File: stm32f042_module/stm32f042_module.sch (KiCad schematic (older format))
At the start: 6 parts, among them P1 CONN_01X10, U1 STM32F042F6P6

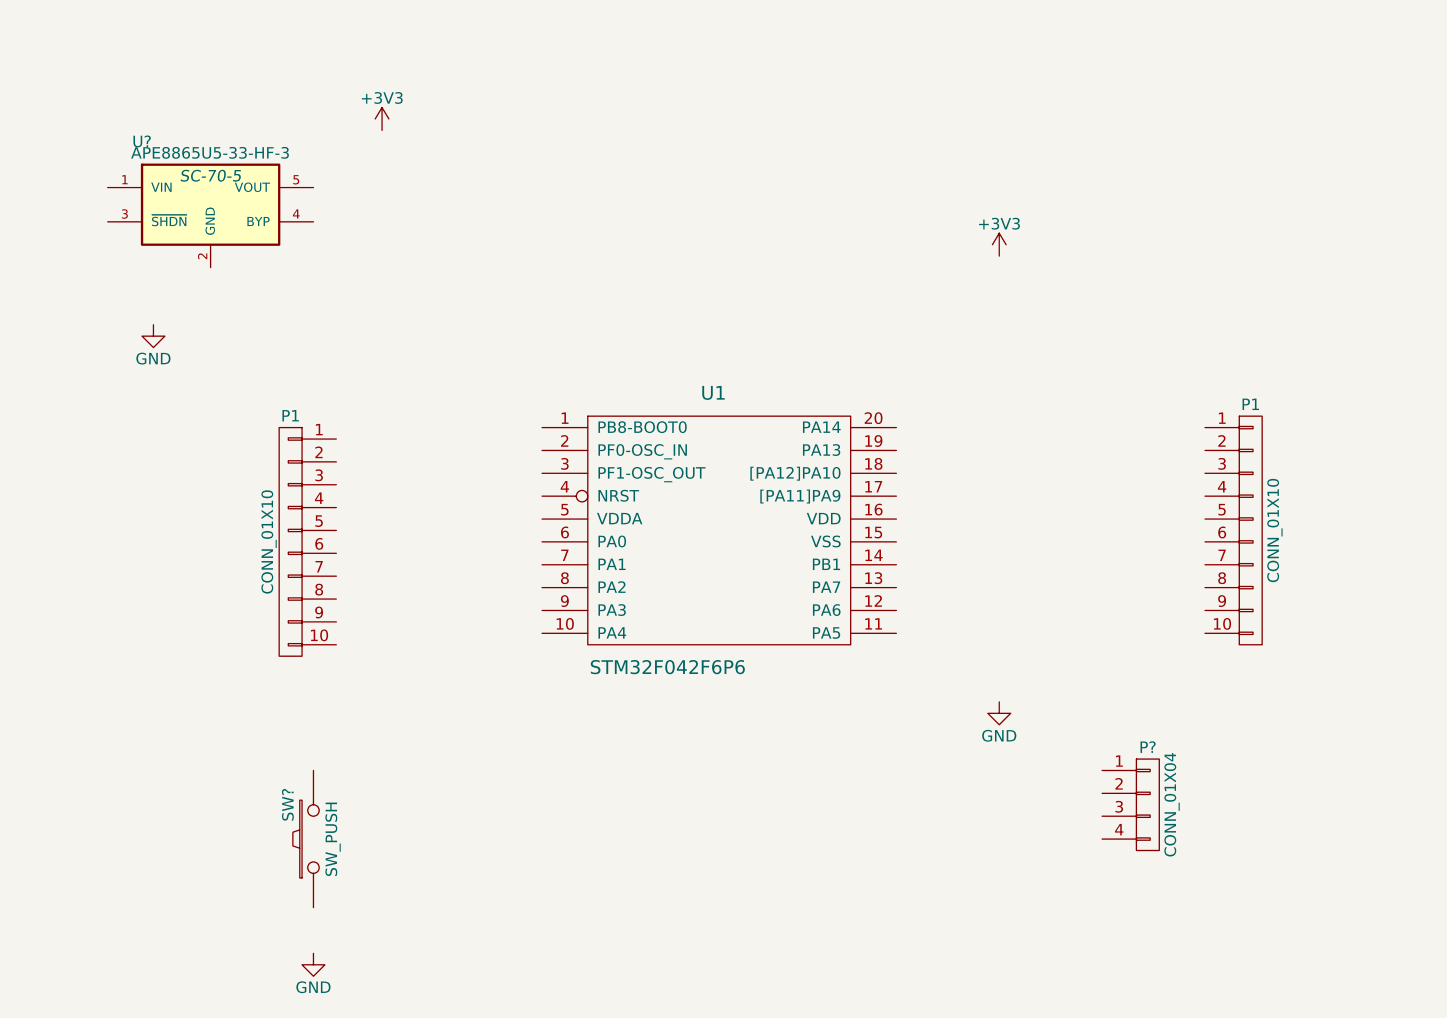
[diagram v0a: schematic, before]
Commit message: add usb conn and footprint
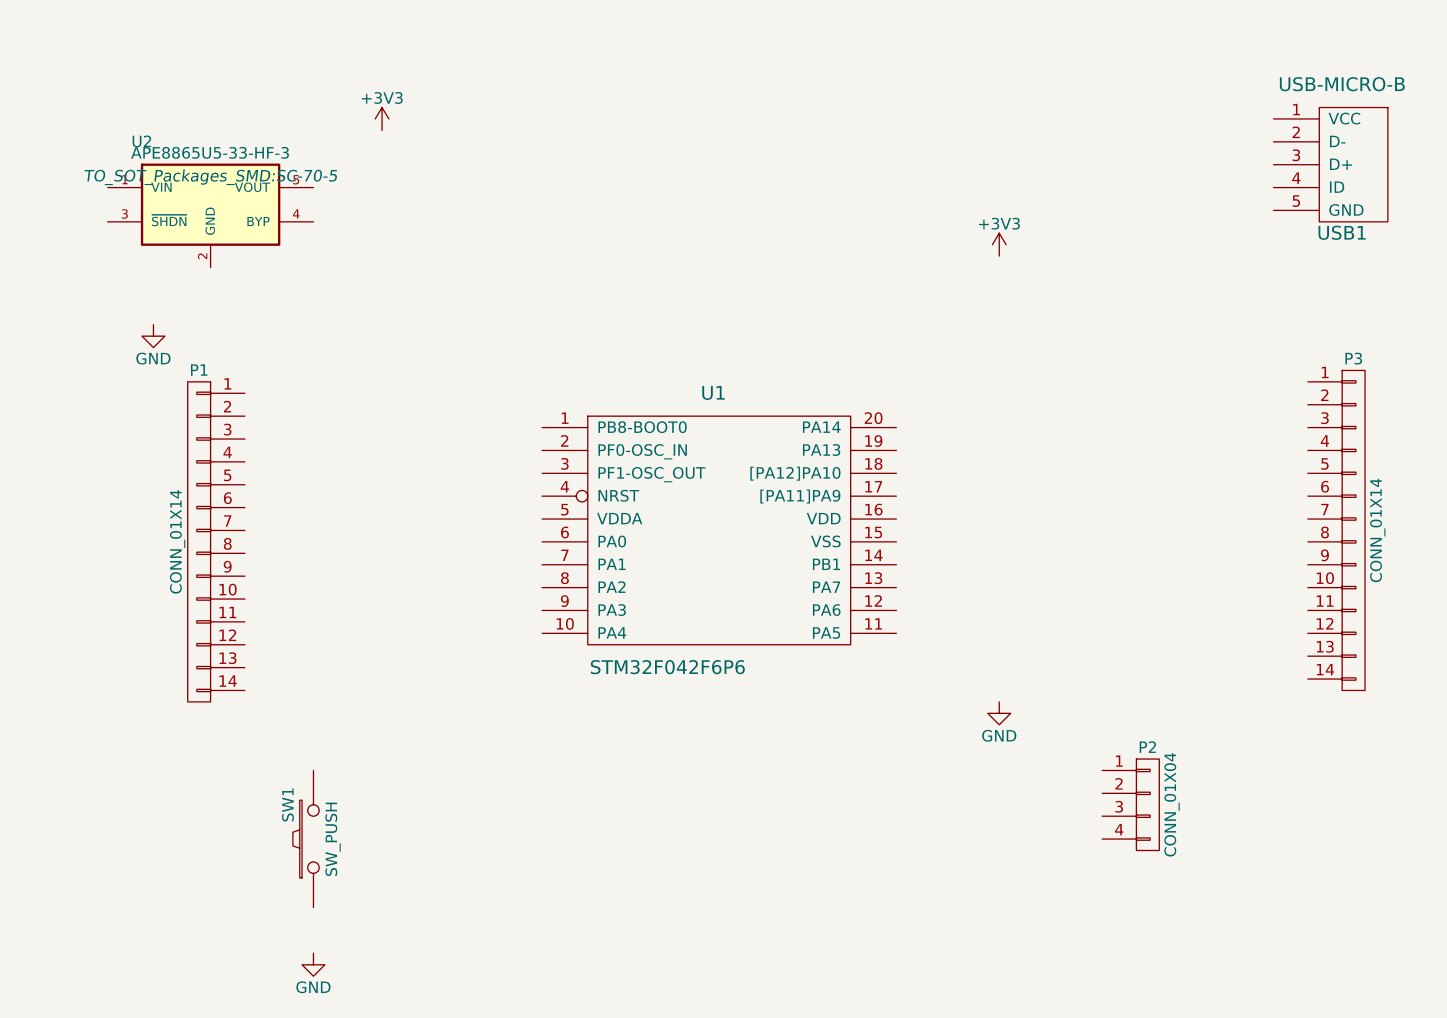
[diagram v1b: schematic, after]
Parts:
- removed P1 (x2): CONN_01X10, symbol CONN_01X10
- added P1, P3: CONN_01X14, symbol CONN_01X14
- added USB1: USB-MICRO-B, smt-other:USB-MICRO-B-SMT, symbol USB-MICRO-B
- U2: renamed from U?; footprint SC-70-5 -> TO_SOT_Packages_SMD:SC-70-5
- gave numbers to parts that had none: 2
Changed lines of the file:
@@
 LIBS:contrib
 LIBS:valves
+LIBS:stm32f042_module-cache
 EELAYER 25 0
 EELAYER END
@@
 $EndComp
 $Comp
-L CONN_01X10 P1
-U 1 1 56DF4BA2
-P 7300 3650
-F 0 "P1" H 7300 4200 50  0000 C CNN
-F 1 "CONN_01X10" V 7400 3650 50  0000 C CNN
-F 2 "" H 7300 3650 50  0000 C CNN
-F 3 "" H 7300 3650 50  0000 C CNN
-	1    7300 3650
-	1    0    0    -1
-$EndComp
-$Comp
-L CONN_01X10 P1
-U 1 1 56DF4C87
-P 3100 3700
-F 0 "P1" H 3100 4250 50  0000 C CNN
-F 1 "CONN_01X10" V 3200 3700 50  0000 C CNN
-F 2 "" H 3100 3700 50  0000 C CNN
-F 3 "" H 3100 3700 50  0000 C CNN
-	1    3100 3700
-	-1   0    0    -1
-$EndComp
-$Comp
-L CONN_01X04 P?
+L CONN_01X04 P2
 U 1 1 56DF4DE3
 P 6850 4850
-F 0 "P?" H 6850 5100 50  0000 C CNN
+F 0 "P2" H 6850 5100 50  0000 C CNN
 F 1 "CONN_01X04" V 6950 4850 50  0000 C CNN
-F 2 "" H 6850 4850 50  0000 C CNN
+F 2 "" H 6850 4850 50  0001 C CNN
 F 3 "" H 6850 4850 50  0000 C CNN
 	1    6850 4850
@@
 $EndComp
 $Comp
-L APE8865U5-33-HF-3 U?
+L APE8865U5-33-HF-3 U2
 U 1 1 56DF4F39
 P 2750 2200
-F 0 "U?" H 2450 2450 50  0000 C CNN
+F 0 "U2" H 2450 2450 50  0000 C CNN
 F 1 "APE8865U5-33-HF-3" H 2750 2400 50  0000 C CNN
-F 2 "SC-70-5" H 2750 2300 50  0000 C CIN
+F 2 "TO_SOT_Packages_SMD:SC-70-5" H 2750 2300 50  0000 C CIN
 F 3 "" H 2750 2200 50  0000 C CNN
 	1    2750 2200
@@
 $EndComp
 $Comp
-L SW_PUSH SW?
+L SW_PUSH SW1
 U 1 1 56DF5011
 P 3200 5000
-F 0 "SW?" H 3350 5110 50  0000 C CNN
+F 0 "SW1" H 3350 5110 50  0000 C CNN
 F 1 "SW_PUSH" H 3200 4920 50  0000 C CNN
-F 2 "" H 3200 5000 50  0000 C CNN
+F 2 "" H 3200 5000 50  0001 C CNN
 F 3 "" H 3200 5000 50  0000 C CNN
 	1    3200 5000
@@
 $EndComp
 $Comp
-L GND #PWR?
+L GND #PWR1
 U 1 1 56DF5317
 P 2500 2750
-F 0 "#PWR?" H 2500 2500 50  0001 C CNN
+F 0 "#PWR1" H 2500 2500 50  0001 C CNN
 F 1 "GND" H 2500 2600 50  0000 C CNN
 F 2 "" H 2500 2750 50  0000 C CNN
@@
 $EndComp
 $Comp
-L GND #PWR?
+L GND #PWR5
 U 1 1 56DF5337
 P 6200 4400
-F 0 "#PWR?" H 6200 4150 50  0001 C CNN
+F 0 "#PWR5" H 6200 4150 50  0001 C CNN
 F 1 "GND" H 6200 4250 50  0000 C CNN
 F 2 "" H 6200 4400 50  0000 C CNN
@@
 $EndComp
 $Comp
-L GND #PWR?
+L GND #PWR2
 U 1 1 56DF536F
 P 3200 5500
-F 0 "#PWR?" H 3200 5250 50  0001 C CNN
+F 0 "#PWR2" H 3200 5250 50  0001 C CNN
 F 1 "GND" H 3200 5350 50  0000 C CNN
 F 2 "" H 3200 5500 50  0000 C CNN
@@
 $EndComp
 $Comp
-L +3V3 #PWR?
+L +3V3 #PWR3
 U 1 1 56DF54F1
 P 3500 1900
-F 0 "#PWR?" H 3500 1750 50  0001 C CNN
+F 0 "#PWR3" H 3500 1750 50  0001 C CNN
 F 1 "+3V3" H 3500 2040 50  0000 C CNN
 F 2 "" H 3500 1900 50  0000 C CNN
@@
 $EndComp
 $Comp
-L +3V3 #PWR?
+L +3V3 #PWR4
 U 1 1 56DF5511
 P 6200 2450
-F 0 "#PWR?" H 6200 2300 50  0001 C CNN
+F 0 "#PWR4" H 6200 2300 50  0001 C CNN
 F 1 "+3V3" H 6200 2590 50  0000 C CNN
 F 2 "" H 6200 2450 50  0000 C CNN
@@
 	1    0    0    -1
 $EndComp
+$Comp
+L CONN_01X14 P3
+U 1 1 56E1F881
+P 7750 3650
+F 0 "P3" H 7750 4400 50  0000 C CNN
+F 1 "CONN_01X14" V 7850 3650 50  0000 C CNN
+F 2 "" H 7750 3650 50  0001 C CNN
+F 3 "" H 7750 3650 50  0000 C CNN
+	1    7750 3650
+	1    0    0    -1
+$EndComp
+$Comp
+L CONN_01X14 P1
+U 1 1 56E1F99E
+P 2700 3700
+F 0 "P1" H 2700 4450 50  0000 C CNN
+F 1 "CONN_01X14" V 2800 3700 50  0000 C CNN
+F 2 "" H 2700 3700 50  0001 C CNN
+F 3 "" H 2700 3700 50  0000 C CNN
+	1    2700 3700
+	-1   0    0    -1
+$EndComp
+$Comp
+L USB-MICRO-B USB1
+U 1 1 56E205A6
+P 7700 2300
+F 0 "USB1" H 7700 2250 60  0000 C CNN
+F 1 "USB-MICRO-B" H 7700 2900 60  0000 C CNN
+F 2 "smt-other:USB-MICRO-B-SMT" H 7700 2250 60  0001 C CNN
+F 3 "" H 7700 2250 60  0000 C CNN
+	1    7700 2300
+	-1   0    0    -1
+$EndComp
 $EndSCHEMATC

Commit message: start design pcb
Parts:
- added C1, C2: 10p, Capacitors_SMD:C_0603_HandSoldering, symbol C
- added C3, C4: 4u7, Capacitors_SMD:C_0603_HandSoldering, symbol CP
- added C5: 100n, Capacitors_SMD:C_0603_HandSoldering, symbol C
- added P4: CONN_01X03, Pin_Headers:Pin_Header_Straight_1x03, symbol CONN_01X03
- added R1, R2: 27R, Resistors_SMD:R_0603_HandSoldering, symbol R
- added R3: 1k5, Resistors_SMD:R_0603_HandSoldering, symbol R
- added X1: 8.000Mhz, smt-other:SMT_5032, symbol Crystal_Small
- P1, P3: footprint (none) -> Pin_Headers:Pin_Header_Straight_1x14
- P2: footprint (none) -> Pin_Headers:Pin_Header_Straight_1x04
- SW1: value SW_PUSH -> RESET; footprint (none) -> smt-other:MICROSWITCH-3x6
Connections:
- net +3V3: now also P1.2 (P2), P1.7 (P7), P2.4 (P4), P3.2 (P2), P3.7 (P7), U1.16 (VDD), U1.5 (VDDA), U2.5 (VOUT), C4.1, C5.2, P4.1 (P1), R3.2
- net GND: now also P1.13 (P13), P1.14 (P14), P2.1 (P1), P3.13 (P13), P3.14 (P14), P3.8 (P8), SW1.2, U1.15 (VSS), U2.2 (GND), USB1.5 (GND), C1.1, C2.1, C3.2, C4.2, C5.1, P4.3 (P3)
- net at U1.1 (PB8-BOOT0): now also P1.3 (P3), P4.2 (P2)
- net at U1.10 (PA4): now also P1.12 (P12)
- net at U1.11 (PA5): now also P3.12 (P12)
- net at U1.12 (PA6): now also P3.11 (P11)
- net at U1.13 (PA7): now also P3.10 (P10)
- net at U1.14 (PB1): now also P3.9 (P9)
- net at U1.17 ([PA11]PA9): now also P3.6 (P6), R1.2
- net at U1.18 ([PA12]PA10): now also P3.5 (P5), R2.2
- net at U1.19 (PA13): now also P2.3 (P3), P3.4 (P4)
- net at U1.2 (PF0-OSC_IN): now also P1.4 (P4), C2.2, X1.1
- net at U1.20 (PA14): now also P2.2 (P2), P3.3 (P3)
- net at U1.3 (PF1-OSC_OUT): now also P1.5 (P5), C1.2, X1.2
- net at U1.4 (NRST): now also P1.6 (P6), SW1.1
- net at U1.6 (PA0): now also P1.8 (P8)
- net at U1.7 (PA1): now also P1.9 (P9)
- net at U1.8 (PA2): now also P1.10 (P10)
- net at U1.9 (PA3): now also P1.11 (P11)
- net +5V: now reaches U2.1 (VIN)
- net +5V: now also P1.1 (P1), P3.1 (P1), U2.3 (~SHDN~), USB1.1 (VCC), C3.1
- net at USB1.2 (D-): now also R1.1
- net at USB1.3 (D+): now also R2.1, R3.1
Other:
- moved on the sheet: P1, P2, P3, SW1
